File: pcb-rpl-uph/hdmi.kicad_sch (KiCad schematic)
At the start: 1 part, among them J11 HDMI_A_1.4

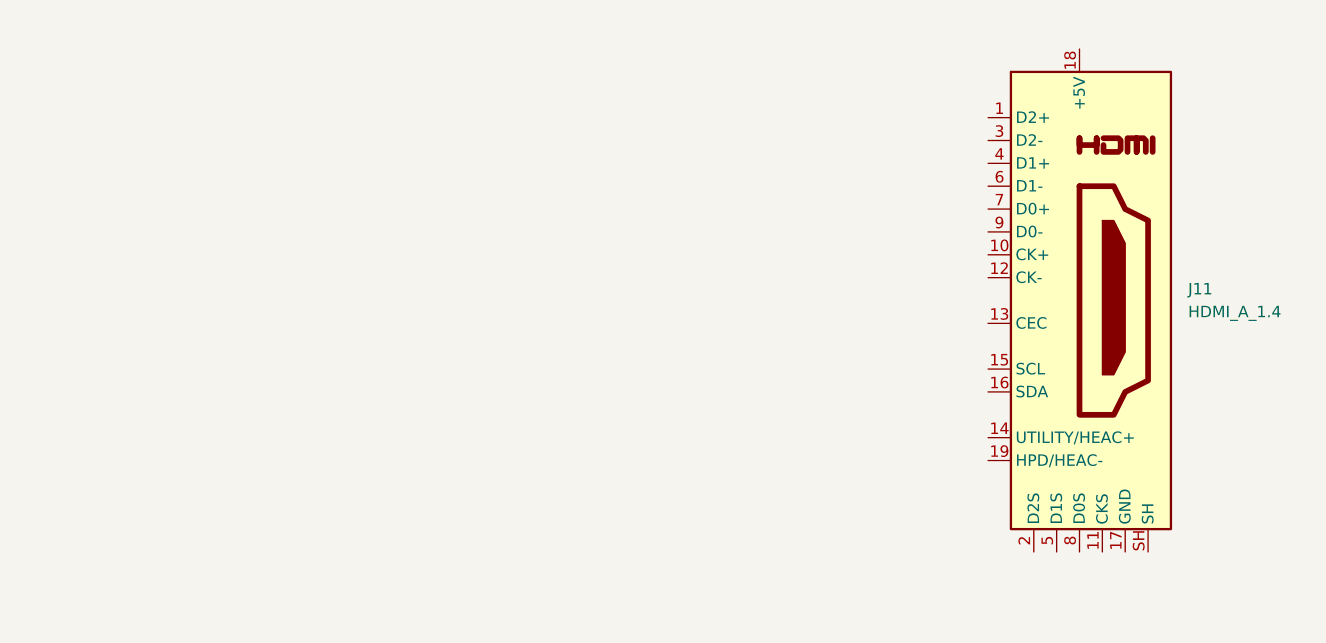
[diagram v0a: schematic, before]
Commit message: Connect CPU HDMI to port
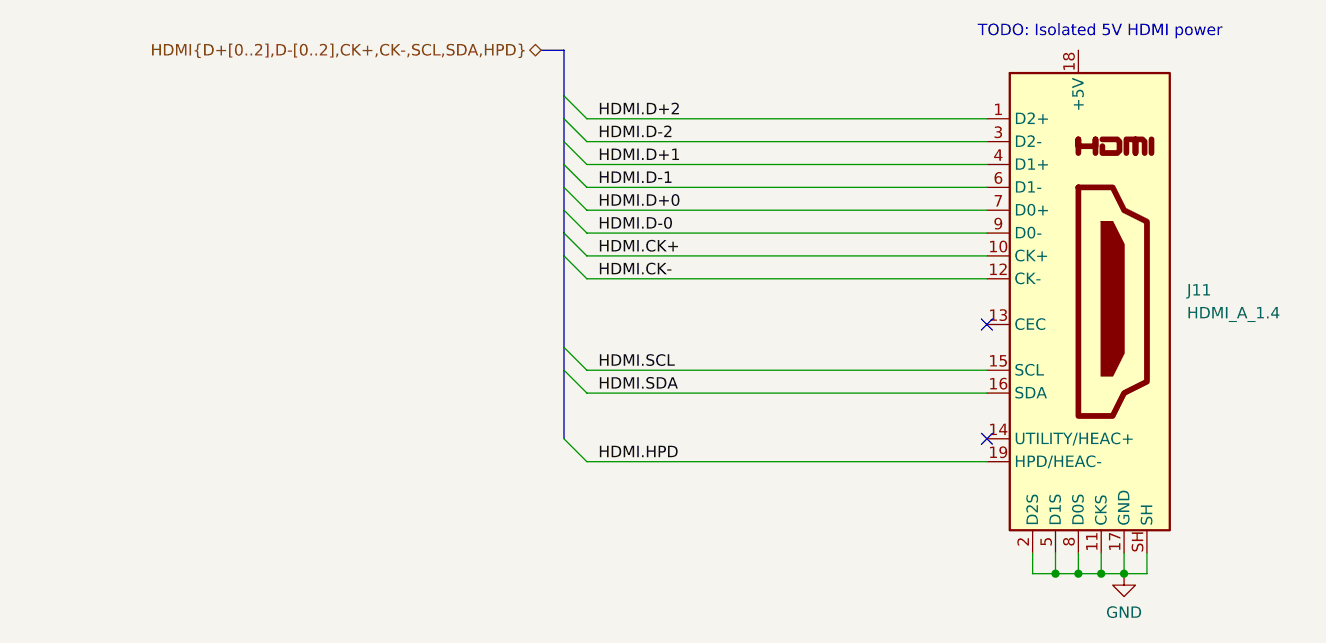
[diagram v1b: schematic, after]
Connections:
- net HDMI.D+2: now reaches J11.1 (D2+)
- net HDMI.CK+: now reaches J11.10 (CK+)
- net GND: now reaches J11.11 (CKS)
- net GND: now also J11.17 (GND), J11.2 (D2S), J11.5 (D1S), J11.8 (D0S), J11.SH
- net HDMI.CK-: now reaches J11.12 (CK-)
- net HDMI.SCL: now reaches J11.15 (SCL)
- net HDMI.SDA: now reaches J11.16 (SDA)
- net HDMI.HPD: now reaches J11.19 (HPD/HEAC-)
- net HDMI.D-2: now reaches J11.3 (D2-)
- net HDMI.D+1: now reaches J11.4 (D1+)
- net HDMI.D-1: now reaches J11.6 (D1-)
- net HDMI.D+0: now reaches J11.7 (D0+)
- net HDMI.D-0: now reaches J11.9 (D0-)
- no-connect marks 0 -> 2
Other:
- note added: "TODO: Isolated 5V HDMI power"
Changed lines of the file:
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@@
 (kicad_sch (version 20230121) (generator eeschema)
   (paper "A4")
-  (symbol (lib_id "Connector:HDMI_A_1.4") (at 159.385 76.835 0) (unit 1)
+  (junction (at 164.338 107.188) (diameter 0) (color 0 0 0 0)
+  )
+  (junction (at 161.798 107.188) (diameter 0) (color 0 0 0 0)
+  )
+  (junction (at 159.258 107.188) (diameter 0) (color 0 0 0 0)
+  )
+  (junction (at 156.718 107.188) (diameter 0) (color 0 0 0 0)
+  )
+  (no_connect (at 149.098 79.502))
+  (no_connect (at 149.098 92.202))
+  (bus_entry (at 102.108 61.722) (size 2.54 2.54)
+    (stroke (width 0) (type default))
+  )
+  (bus_entry (at 102.108 82.042) (size 2.54 2.54)
+    (stroke (width 0) (type default))
+  )
+  (bus_entry (at 102.108 69.342) (size 2.54 2.54)
+    (stroke (width 0) (type default))
+  )
+  (bus_entry (at 102.108 64.262) (size 2.54 2.54)
+    (stroke (width 0) (type default))
+  )
+  (bus_entry (at 102.108 56.642) (size 2.54 2.54)
+    (stroke (width 0) (type default))
+  )
+  (bus_entry (at 102.108 54.102) (size 2.54 2.54)
+    (stroke (width 0) (type default))
+  )
+  (bus_entry (at 102.108 92.202) (size 2.54 2.54)
+    (stroke (width 0) (type default))
+  )
+  (bus_entry (at 102.108 66.802) (size 2.54 2.54)
+    (stroke (width 0) (type default))
+  )
+  (bus_entry (at 102.108 71.882) (size 2.54 2.54)
+    (stroke (width 0) (type default))
+  )
+  (bus_entry (at 102.108 59.182) (size 2.54 2.54)
+    (stroke (width 0) (type default))
+  )
+  (bus_entry (at 102.108 84.582) (size 2.54 2.54)
+    (stroke (width 0) (type default))
+  )
+  (wire (pts (xy 161.798 104.902) (xy 161.798 107.188))
+    (stroke (width 0) (type default))
+  )
+  (wire (pts (xy 166.878 104.902) (xy 166.878 107.188))
+    (stroke (width 0) (type default))
+  )
+  (bus (pts (xy 102.108 71.882) (xy 102.108 69.342))
+    (stroke (width 0) (type default))
+  )
+  (bus (pts (xy 102.108 54.102) (xy 102.108 49.022))
+    (stroke (width 0) (type default))
+  )
+  (bus (pts (xy 102.108 49.022) (xy 99.568 49.022))
+    (stroke (width 0) (type default))
+  )
+  (wire (pts (xy 104.648 71.882) (xy 149.098 71.882))
+    (stroke (width 0) (type default))
+  )
+  (wire (pts (xy 104.648 64.262) (xy 149.098 64.262))
+    (stroke (width 0) (type default))
+  )
+  (wire (pts (xy 156.718 104.902) (xy 156.718 107.188))
+    (stroke (width 0) (type default))
+  )
+  (wire (pts (xy 104.648 94.742) (xy 149.098 94.742))
+    (stroke (width 0) (type default))
+  )
+  (wire (pts (xy 161.798 107.188) (xy 164.338 107.188))
+    (stroke (width 0) (type default))
+  )
+  (wire (pts (xy 104.648 56.642) (xy 149.098 56.642))
+    (stroke (width 0) (type default))
+  )
+  (wire (pts (xy 104.648 74.422) (xy 149.098 74.422))
+    (stroke (width 0) (type default))
+  )
+  (wire (pts (xy 104.648 59.182) (xy 149.098 59.182))
+    (stroke (width 0) (type default))
+  )
+  (wire (pts (xy 104.648 66.802) (xy 149.098 66.802))
+    (stroke (width 0) (type default))
+  )
+  (bus (pts (xy 102.108 69.342) (xy 102.108 66.802))
+    (stroke (width 0) (type default))
+  )
+  (wire (pts (xy 159.258 107.188) (xy 161.798 107.188))
+    (stroke (width 0) (type default))
+  )
+  (bus (pts (xy 102.108 64.262) (xy 102.108 61.722))
+    (stroke (width 0) (type default))
+  )
+  (wire (pts (xy 154.178 104.902) (xy 154.178 107.188))
+    (stroke (width 0) (type default))
+  )
+  (wire (pts (xy 104.648 84.582) (xy 149.098 84.582))
+    (stroke (width 0) (type default))
+  )
+  (bus (pts (xy 102.108 71.882) (xy 102.108 82.042))
+    (stroke (width 0) (type default))
+  )
+  (wire (pts (xy 159.258 104.902) (xy 159.258 107.188))
+    (stroke (width 0) (type default))
+  )
+  (wire (pts (xy 156.718 107.188) (xy 159.258 107.188))
+    (stroke (width 0) (type default))
+  )
+  (wire (pts (xy 104.648 69.342) (xy 149.098 69.342))
+    (stroke (width 0) (type default))
+  )
+  (bus (pts (xy 102.108 66.802) (xy 102.108 64.262))
+    (stroke (width 0) (type default))
+  )
+  (wire (pts (xy 104.648 61.722) (xy 149.098 61.722))
+    (stroke (width 0) (type default))
+  )
+  (wire (pts (xy 104.648 87.122) (xy 149.098 87.122))
+    (stroke (width 0) (type default))
+  )
+  (bus (pts (xy 102.108 59.182) (xy 102.108 56.642))
+    (stroke (width 0) (type default))
+  )
+  (bus (pts (xy 102.108 84.582) (xy 102.108 82.042))
+    (stroke (width 0) (type default))
+  )
+  (wire (pts (xy 154.178 107.188) (xy 156.718 107.188))
+    (stroke (width 0) (type default))
+  )
+  (bus (pts (xy 102.108 84.582) (xy 102.108 92.202))
+    (stroke (width 0) (type default))
+  )
+  (bus (pts (xy 102.108 56.642) (xy 102.108 54.102))
+    (stroke (width 0) (type default))
+  )
+  (wire (pts (xy 166.878 107.188) (xy 164.338 107.188))
+    (stroke (width 0) (type default))
+  )
+  (wire (pts (xy 164.338 104.902) (xy 164.338 107.188))
+    (stroke (width 0) (type default))
+  )
+  (bus (pts (xy 102.108 61.722) (xy 102.108 59.182))
+    (stroke (width 0) (type default))
+  )
+  (text "TODO: Isolated 5V HDMI power" (at 148.082 47.752 0)
+    (effects (font (size 1.27 1.27)) (justify left bottom))
+  )
+  (label "HDMI.CK-" (at 105.918 74.422 0) (fields_autoplaced)
+    (effects (font (size 1.27 1.27)) (justify left bottom))
+  )
+  (label "HDMI.D-0" (at 105.918 69.342 0) (fields_autoplaced)
+    (effects (font (size 1.27 1.27)) (justify left bottom))
+  )
+  (label "HDMI.HPD" (at 105.918 94.742 0) (fields_autoplaced)
+    (effects (font (size 1.27 1.27)) (justify left bottom))
+  )
+  (label "HDMI.D+0" (at 105.918 66.802 0) (fields_autoplaced)
+    (effects (font (size 1.27 1.27)) (justify left bottom))
+  )
+  (label "HDMI.D-2" (at 105.918 59.182 0) (fields_autoplaced)
+    (effects (font (size 1.27 1.27)) (justify left bottom))
+  )
+  (label "HDMI.D+1" (at 105.918 61.722 0) (fields_autoplaced)
+    (effects (font (size 1.27 1.27)) (justify left bottom))
+  )
+  (label "HDMI.CK+" (at 105.918 71.882 0) (fields_autoplaced)
+    (effects (font (size 1.27 1.27)) (justify left bottom))
+  )
+  (label "HDMI.SCL" (at 105.918 84.582 0) (fields_autoplaced)
+    (effects (font (size 1.27 1.27)) (justify left bottom))
+  )
+  (label "HDMI.SDA" (at 105.918 87.122 0) (fields_autoplaced)
+    (effects (font (size 1.27 1.27)) (justify left bottom))
+  )
+  (label "HDMI.D-1" (at 105.918 64.262 0) (fields_autoplaced)
+    (effects (font (size 1.27 1.27)) (justify left bottom))
+  )
+  (label "HDMI.D+2" (at 105.918 56.642 0) (fields_autoplaced)
+    (effects (font (size 1.27 1.27)) (justify left bottom))
+  )
+  (hierarchical_label "HDMI{D+[0..2],D-[0..2],CK+,CK-,SCL,SDA,HPD}" (shape bidirectional) (at 99.568 49.022 180) (fields_autoplaced)
+    (effects (font (size 1.27 1.27)) (justify right))
+  )
+  (symbol (lib_id "power:GND") (at 164.338 107.188 0) (unit 1)
     (in_bom yes) (on_board yes) (dnp no) (fields_autoplaced)
-    (property "Reference" "J11" (at 171.45 75.565 0)
+    (property "Reference" "#PWR017" (at 164.338 113.538 0)
+      (effects (font (size 1.27 1.27)) hide)
+    )
+    (property "Value" "GND" (at 164.338 111.506 0)
+      (effects (font (size 1.27 1.27)))
+    )
+    (property "Footprint" "" (at 164.338 107.188 0)
+      (effects (font (size 1.27 1.27)) hide)
+    )
+    (property "Datasheet" "" (at 164.338 107.188 0)
+      (effects (font (size 1.27 1.27)) hide)
+    )
+    (pin "1")
+    (instances
+      (project "virgo-rpl-uph"
+        (path "/16b1e6ca-a3e2-42a7-b57e-a744c26a548a/e06851b0-7731-40a5-abc7-af16a010e494"
+          (reference "#PWR017") (unit 1)
+        )
+      )
+    )
+  )
+  (symbol (lib_id "Connector:HDMI_A_1.4") (at 159.258 76.962 0) (unit 1)
+    (in_bom yes) (on_board yes) (dnp no) (fields_autoplaced)
+    (property "Reference" "J11" (at 171.323 75.692 0)
       (effects (font (size 1.27 1.27)) (justify left))
     )
-    (property "Value" "HDMI_A_1.4" (at 171.45 78.105 0)
+    (property "Value" "HDMI_A_1.4" (at 171.323 78.232 0)
       (effects (font (size 1.27 1.27)) (justify left))
     )
-    (property "Footprint" "Connector_HDMI:HDMI_A_Molex_208658-1001_Horizontal" (at 160.02 76.835 0)
-      (effects (font (size 1.27 1.27)) hide)
-    )
-    (property "Datasheet" "https://en.wikipedia.org/wiki/HDMI" (at 160.02 76.835 0)
-      (effects (font (size 1.27 1.27)) hide)
-    )
+    (property "Footprint" "Connector_HDMI:HDMI_A_Molex_208658-1001_Horizontal" (at 159.893 76.962 0)
+      (effects (font (size 1.27 1.27)) hide)
+    )
+    (property "Datasheet" "https://en.wikipedia.org/wiki/HDMI" (at 159.893 76.962 0)
+      (effects (font (size 1.27 1.27)) hide)
+    )

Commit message: refactor much of CPU schematic symbol
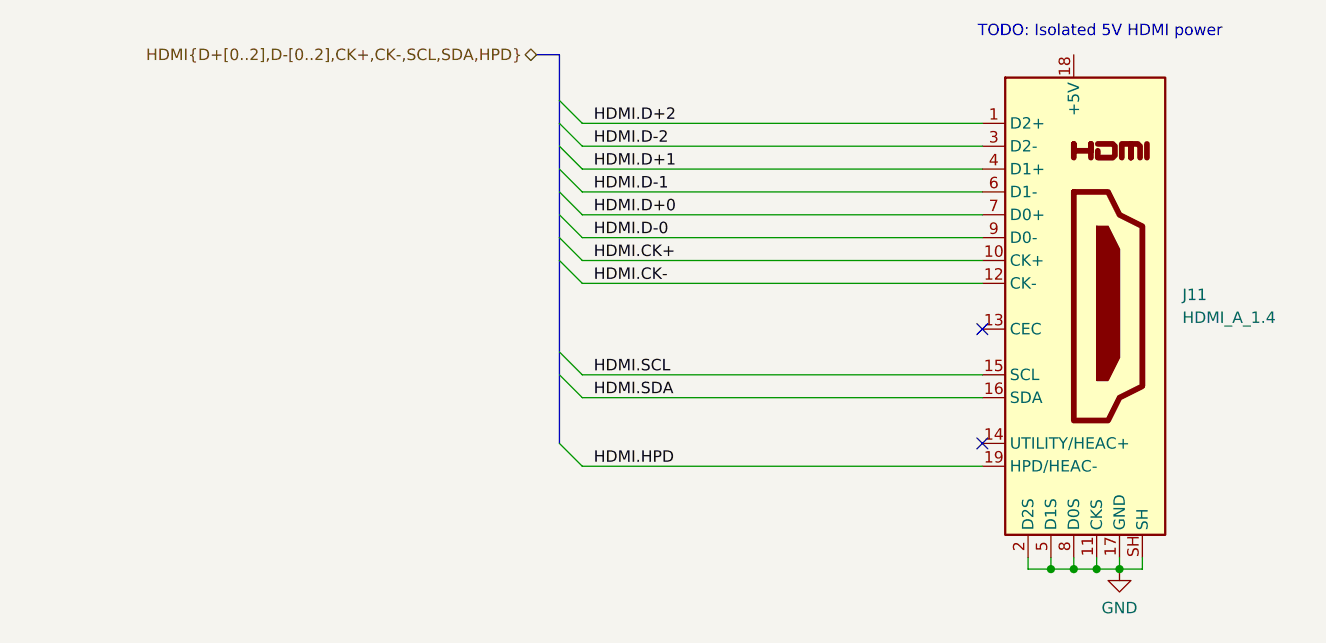
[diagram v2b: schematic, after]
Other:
- moved on the sheet: J11
